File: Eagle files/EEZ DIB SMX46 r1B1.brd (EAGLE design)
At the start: 146 x 95 mm, 157 parts, among them IC1 STM32F030C6T6, IC2 74HC1G126DBVT, IC3 M24C32-WMN6P, IC4 LP2985-33DBVR, IC5 74HC2G04GW,125, K1 FTR-C1GA012G-B05, K10 FTR-C1GA012G-B05, K11 FTR-C1GA012G-B05, K12 FTR-C1GA012G-B05, K13 FTR-C1GA012G-B05, K14 FTR-C1GA012G-B05, K15 FTR-C1GA012G-B05, K16 FTR-C1GA012G-B05, K17 FTR-C1GA012G-B05, K18 FTR-C1GA012G-B05, K19 FTR-C1GA012G-B05, K2 FTR-C1GA012G-B05, K20 FTR-C1GA012G-B05, K21 FTR-C1GA012G-B05, K22 FTR-C1GA012G-B05, K23 FTR-C1GA012G-B05, K24 FTR-C1GA012G-B05, K3 FTR-C1GA012G-B05, K4 FTR-C1GA012G-B05, K5 FTR-C1GA012G-B05, K6 FTR-C1GA012G-B05, K7 FTR-C1GA012G-B05, K8 FTR-C1GA012G-B05, K9 FTR-C1GA012G-B05, Q1 2N7002, Q10 2N7002, Q11 2N7002, Q12 2N7002, Q13 2N7002, Q14 2N7002, Q15 2N7002, Q16 2N7002, Q17 2N7002, Q18 2N7002, Q19 2N7002, Q2 2N7002, Q20 2N7002, Q21 2N7002, Q22 2N7002, Q23 2N7002, Q24 2N7002, Q25 2N7002, Q3 2N7002, Q4 2N7002, Q5 2N7002, Q6 2N7002, Q7 2N7002, Q8 2N7002, Q9 2N7002, X1 N.C., X2 77317-104-28LF, X3 691327310016, X4 691327310016

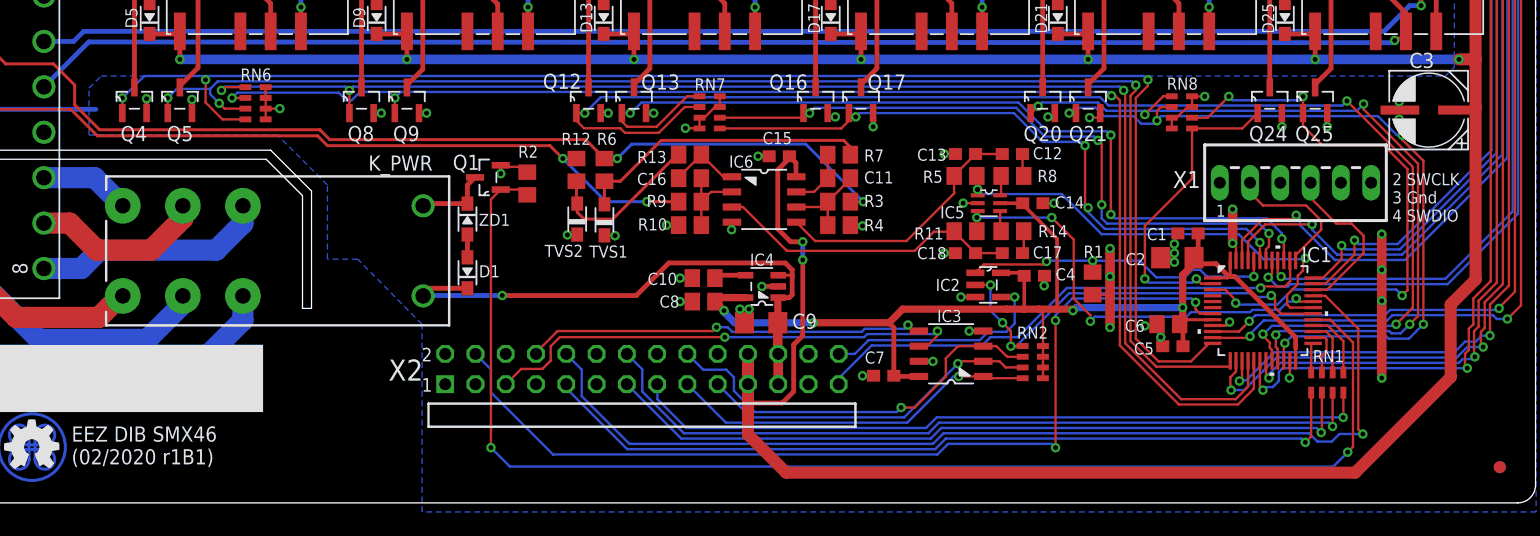
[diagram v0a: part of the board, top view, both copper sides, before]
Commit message: UART relocated
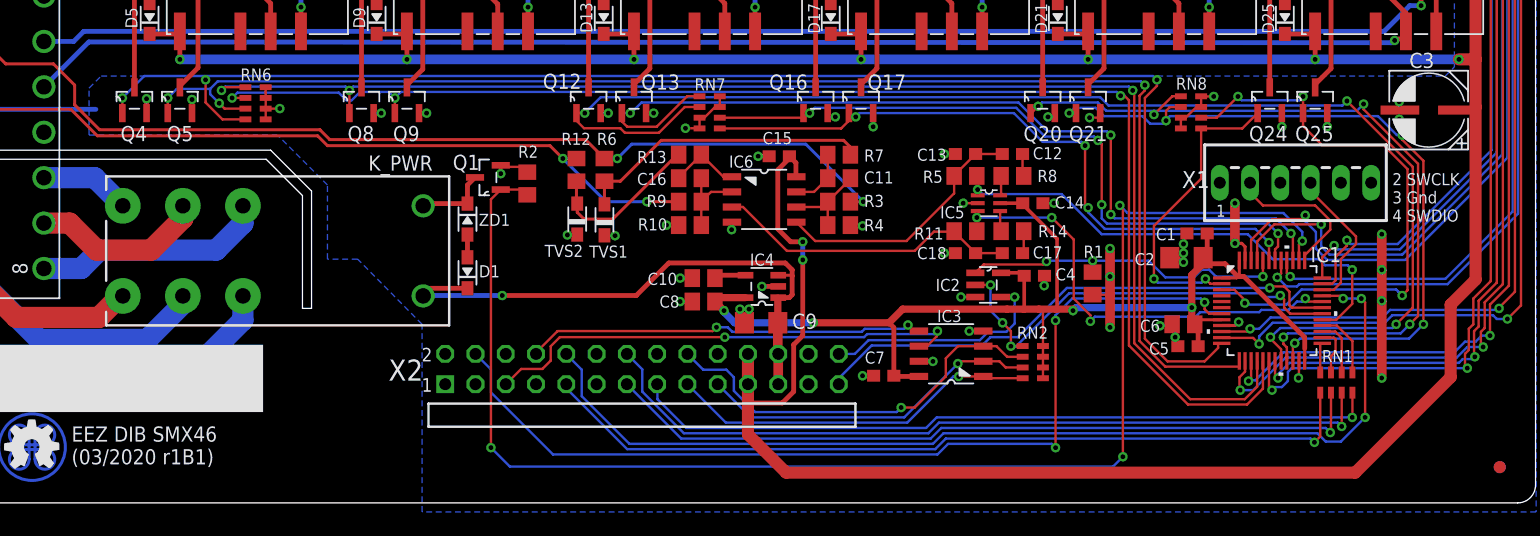
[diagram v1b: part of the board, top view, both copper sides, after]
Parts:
- IC6: value (none) -> OPA2170
- moved C5 1.27 mm to (116.8, 13.1)
- moved C6 1.27 mm to (116.5, 15.0)
- moved C1 0.76 mm to (117.6, 22.6)
- moved C2 0.76 mm to (116.7, 20.6)
- moved IC1 0.76 mm to (123.9, 16.1)
- moved RN1 0.76 mm to (129.3, 10.1)
- moved RN8 0.76 mm to (117.1, 32.8)
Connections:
- net K_PWR: now also IC1.38; no longer IC1.29
- net PWM#1: now also IC1.29; no longer IC1.31
- net UART_RX: now also IC1.31; no longer IC1.38
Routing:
- net K_PWR: track 111.0 -> 118.3 mm, vias 2 -> 4
- net PWM#1: track 38.4 -> 41.8 mm, vias 3 -> 2
- net UART_RX: track 43.5 -> 45.7 mm
- net SWDIO: track 14.0 -> 12.3 mm
- net OUT23: track 51.9 -> 50.3 mm
- net OUT18: track 67.1 -> 65.9 mm
- net +3V3: track 103.0 -> 104.2 mm
- net GND: track 127.1 -> 128.2 mm
- net OUT19: track 63.0 -> 62.0 mm
- net OUT2: track 124.4 -> 125.4 mm
- net SWCLK: track 12.0 -> 12.8 mm
- net OUT9: track 204.0 -> 203.3 mm
- net OUT8: track 187.2 -> 186.5 mm
- net OUT7: track 115.1 -> 115.8 mm
- net OUT6: track 116.4 -> 117.1 mm
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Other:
- board text added: "EEZ DIB SMX46 (03/2020 r1B1)"
- board text added: "EEZ DIB SMX46 (03/2020 r1B1) Project source code: github.com/eez-open"
- board text removed: "EEZ DIB SMX46 (02/2020 r1B1)"
- board text removed: "EEZ DIB SMX46 (02/2020 r1B1) Project source code: github.com/eez-open"

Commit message: debug connector update
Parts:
- X1: value N.C. -> SSW-106-02-S-S; device EEZ_connectors:22-23-2061 -> con-samtec:SSW-106-02-S-S
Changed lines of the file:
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@@
 <attribute name="VALUE" x="94.9071" y="17.907" size="0.6096" layer="27" ratio="10" rot="SR0"/>
 </element>
-<element name="X1" library="EEZ_connectors" package="22-23-2061" value="N.C." x="125.857" y="26.8605" smashed="yes">
-<attribute name="OC_NEWARK" value="27C1933" x="125.857" y="26.8605" size="1.016" layer="27" ratio="10" display="off"/>
-<attribute name="MPN" value="22-23-2061" x="125.857" y="26.8605" size="1.016" layer="27" ratio="10" display="off"/>
-<attribute name="MF" value="MOLEX" x="125.857" y="26.8605" size="1.016" layer="27" ratio="10" display="off"/>
-<attribute name="OC_FARNELL" value="1462922" x="125.857" y="26.8605" size="1.016" layer="27" ratio="10" display="off"/>
-<attribute name="NAME" x="116.332" y="26.416" size="1.4224" layer="25" ratio="10"/>
-<attribute name="VALUE" x="122.9995" y="24.003" size="1.016" layer="27" ratio="10"/>
-</element>
 <element name="RN3" library="EEZ_Lib1" package="CAY16" value="DR1206-47K-4/8" x="57.658" y="89.408" smashed="yes" rot="R90">
 <attribute name="NAME" x="56.4515" y="91.186" size="1.016" layer="25" ratio="10"/>
@@
 <element name="FM2" library="EEZ_Lib1" package="FIDUCIAL_DUAL" value="FIDUCIAL_2" x="143" y="3"/>
 <element name="FM1" library="EEZ_Lib1" package="FIDUCIAL_DUAL" value="FIDUCIAL_2" x="16" y="92"/>
+<element name="X1" library="con-samtec" package="SSW-106-02-S-S" value="SSW-106-02-S-S" x="125.857" y="26.8605" smashed="yes">
+<attribute name="OC_NEWARK" value="11P9416" x="125.857" y="26.8605" size="1.016" layer="27" ratio="10" display="off"/>
+<attribute name="MPN" value="SSW-106-02-S-S" x="125.857" y="26.8605" size="1.016" layer="27" ratio="10" display="off"/>
+<attribute name="MF" value="" x="125.857" y="26.8605" size="1.016" layer="27" ratio="10" display="off"/>
+<attribute name="OC_FARNELL" value="unknown" x="125.857" y="26.8605" size="1.016" layer="27" ratio="10" display="off"/>
+<attribute name="NAME" x="118.11" y="27.4955" size="1.27" layer="25" ratio="10" rot="R180"/>
+<attribute name="VALUE" x="135.382" y="25.5905" size="1.27" layer="27" rot="R90"/>
+</element>
 </elements>
 <signals>
@@
 <contactref element="X4" pad="10"/>
 <contactref element="X4" pad="12"/>
-<contactref element="X1" pad="3"/>
 <contactref element="RN5" pad="4"/>
 <contactref element="RN3" pad="2"/>
@@
 <wire x1="121.6279" y1="21.5011" x2="121.3485" y2="21.7805" width="0.254" layer="1"/>
 <wire x1="121.3485" y1="21.7805" x2="120.777" y2="21.7805" width="0.254" layer="1"/>
+<contactref element="X1" pad="3"/>
 </signal>
 <signal name="N$13">
@@
 <signal name="SWDIO">
 <contactref element="IC1" pad="34"/>
-<contactref element="X1" pad="4"/>
 <wire x1="128.1049" y1="17.8816" x2="129.0701" y2="17.8816" width="0.2032" layer="1"/>
 <wire x1="129.0701" y1="17.8816" x2="129.667" y2="18.4785" width="0.2032" layer="1"/>
@@
 <wire x1="127.127" y1="26.8605" x2="127.127" y2="26.162" width="0.2032" layer="1"/>
 <wire x1="127.127" y1="26.162" x2="130.937" y2="22.352" width="0.2032" layer="1"/>
+<contactref element="X1" pad="4"/>
 </signal>
 <signal name="UART_RX">
@@
 <signal name="SWCLK">
 <contactref element="IC1" pad="37"/>
-<contactref element="X1" pad="2"/>
 <wire x1="126.6317" y1="20.3454" x2="126.6317" y2="20.7772" width="0.2032" layer="1"/>
 <wire x1="126.6317" y1="20.7772" x2="128.778" y2="22.9235" width="0.2032" layer="1"/>
@@
 <wire x1="122.047" y1="26.035" x2="122.047" y2="26.8605" width="0.2032" layer="1"/>
 <wire x1="127.508" y1="24.9555" x2="128.778" y2="23.6855" width="0.2032" layer="1"/>
+<contactref element="X1" pad="2"/>
 </signal>
 <signal name="DIB_NRESET">

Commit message: PCB terminals position adjusted
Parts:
- moved X3 2.20 mm to (12.3, 65.0)
- moved X4 2.20 mm to (12.3, 33.0)
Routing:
- net GND: track 128.2 -> 132.8 mm
- net N$7: track 148.9 -> 151.1 mm
- net N$34: track 117.7 -> 119.9 mm
- net N$16: track 139.4 -> 141.6 mm
- net N$14: track 83.1 -> 85.3 mm
- net N$12: track 139.4 -> 141.6 mm
- net N$11: track 153.7 -> 155.9 mm
- net N$10: track 153.7 -> 155.9 mm
- net N$1: track 63.2 -> 65.4 mm
- net N$95: track 30.3 -> 32.5 mm
- net N$94: track 7.60 -> 9.80 mm
- net N$84: track 19.7 -> 21.9 mm
- net N$82: track 14.8 -> 17.0 mm
- net N$25: track 101.4 -> 103.6 mm
- net N$24: track 101.6 -> 103.8 mm
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
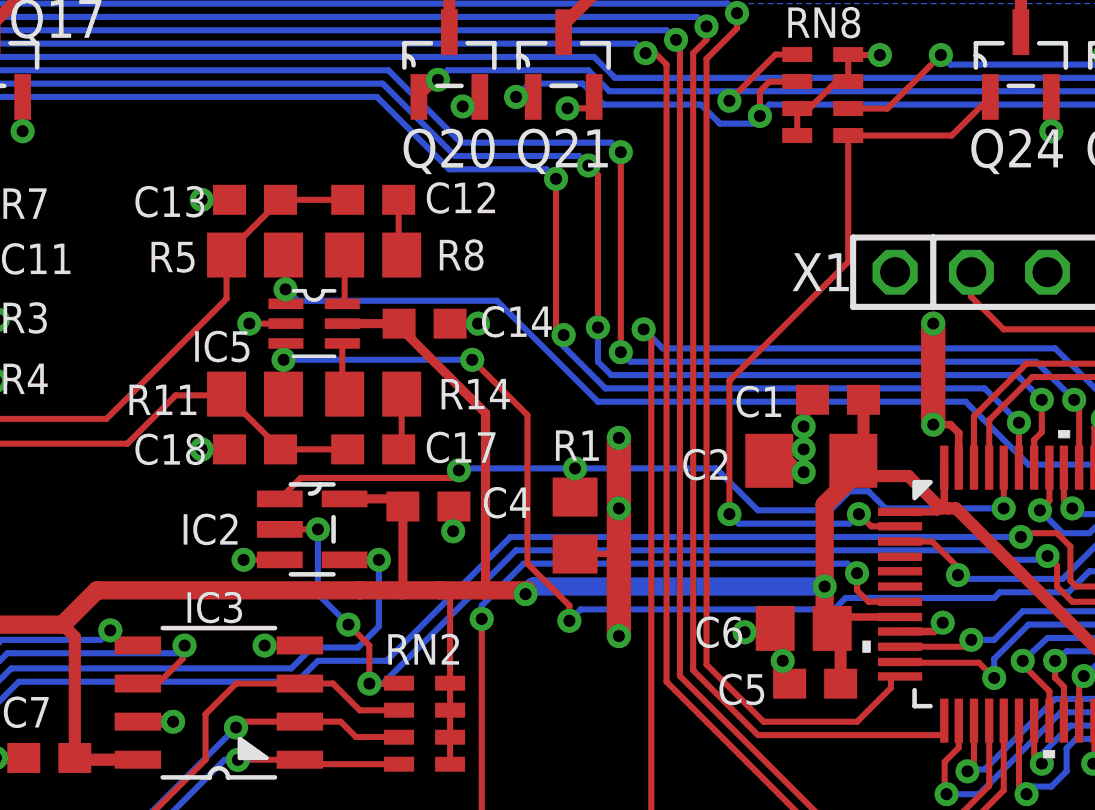
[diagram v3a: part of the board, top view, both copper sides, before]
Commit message: IC2 package update
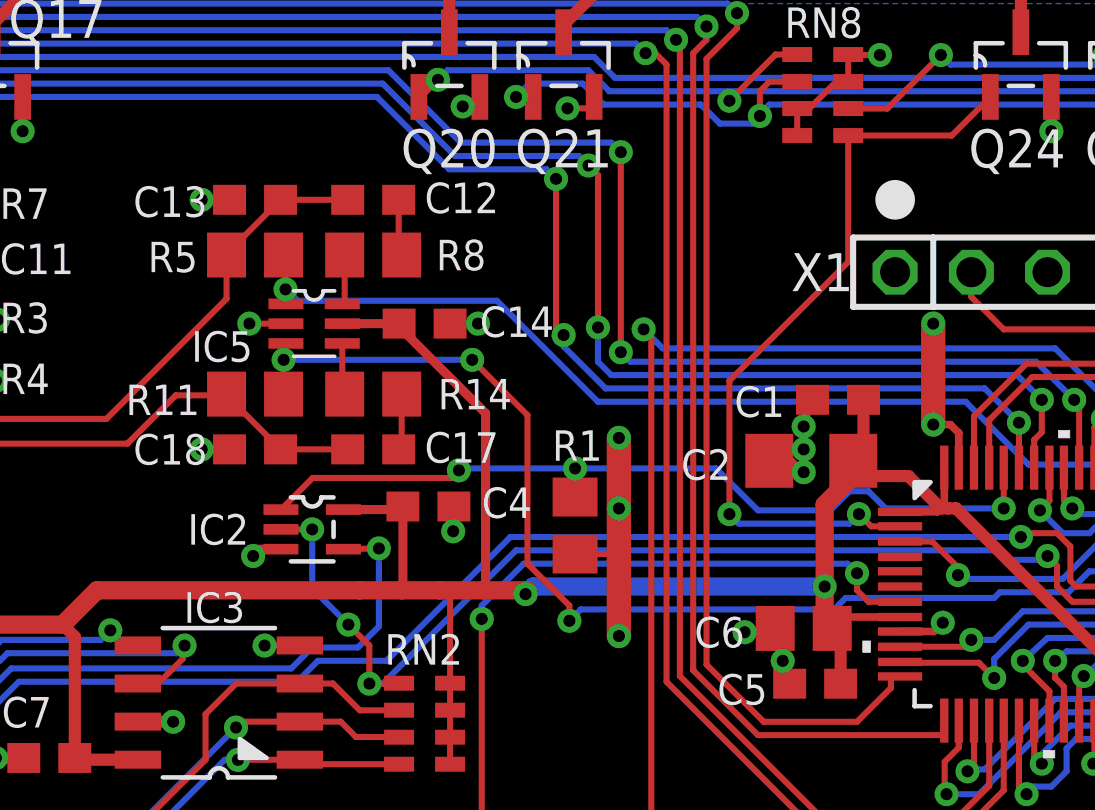
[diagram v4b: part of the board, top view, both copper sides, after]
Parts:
- IC2: value 74HC1G126DBVT -> 74HC1G126GW,125; device EEZ_TI:SOT23-5 -> EEZ_Lib1:SOT65P210X110-5N
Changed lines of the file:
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@@
 <layer number="20" name="Dimension" color="12" fill="1" visible="yes" active="yes"/>
 <layer number="21" name="tPlace" color="7" fill="1" visible="yes" active="yes"/>
-<layer number="22" name="bPlace" color="6" fill="1" visible="yes" active="yes"/>
+<layer number="22" name="bPlace" color="6" fill="1" visible="no" active="yes"/>
 <layer number="23" name="tOrigins" color="15" fill="1" visible="yes" active="yes"/>
 <layer number="24" name="bOrigins" color="15" fill="1" visible="no" active="yes"/>
@@
 4 SWDIO
 </text>
+<circle x="119.507" y="29.2735" radius="0.3302" width="0.6604" layer="21"/>
 </plain>
 <attributes>
@@
 <attribute name="VALUE" x="102.489" y="18.542" size="1.016" layer="27" ratio="10"/>
 </element>
-<element name="IC2" library="EEZ_TI" package="SOT23-5" value="74HC1G126DBVT" x="100.076" y="18.288" smashed="yes">
-<attribute name="NAME" x="95.6691" y="17.78" size="1.016" layer="25" ratio="10" rot="SR0"/>
-<attribute name="VALUE" x="94.9071" y="17.907" size="0.6096" layer="27" ratio="10" rot="SR0"/>
+<element name="IC2" library="EEZ_Lib1" package="SOT65P210X110-5N" value="74HC1G126GW,125" x="100.076" y="18.288" smashed="yes">
+<attribute name="NAME" x="95.9231" y="17.78" size="1.016" layer="25" ratio="10" rot="SR0"/>
+<attribute name="VALUE" x="94.0816" y="18.034" size="0.6096" layer="27" ratio="10" rot="SR0"/>
 </element>
 <element name="RN3" library="EEZ_Lib1" package="CAY16" value="DR1206-47K-4/8" x="57.658" y="89.408" smashed="yes" rot="R90">
@@
 <via x="96.393" y="29.2735" extent="1-16" drill="0.4" shape="square"/>
 <wire x1="97.321" y1="29.2735" x2="96.393" y2="29.2735" width="0.2032" layer="1"/>
-<via x="97.79" y="17.272" extent="1-16" drill="0.4" shape="square"/>
+<via x="98.1075" y="17.399" extent="1-16" drill="0.4" shape="square"/>
 <via x="96.393" y="20.955" extent="1-16" drill="0.4" shape="square"/>
 <wire x1="97.321" y1="20.955" x2="96.393" y2="20.955" width="0.2032" layer="1"/>
-<wire x1="98.9965" y1="17.272" x2="97.79" y2="17.272" width="0.2032" layer="1"/>
 <wire x1="90.463" y1="10.668" x2="89.535" y2="10.668" width="0.4064" layer="1"/>
 <via x="95.4405" y="11.8745" extent="1-16" drill="0.4" shape="square"/>
@@
 <wire x1="8.8265" y1="41.5925" x2="8.8265" y2="33.0835" width="0.4064" layer="16"/>
 <wire x1="8.8265" y1="33.0835" x2="8.89" y2="33.02" width="0.4064" layer="16"/>
+<wire x1="99.0346" y1="17.6276" x2="98.1075" y2="17.6276" width="0.3048" layer="1"/>
+<wire x1="98.1075" y1="17.6276" x2="98.1075" y2="17.399" width="0.3048" layer="1"/>
 </signal>
 <signal name="N$13">
@@
 <wire x1="78.8035" y1="15.113" x2="77.9145" y2="16.002" width="0.6096" layer="16"/>
 <wire x1="77.9145" y1="16.002" x2="77.9145" y2="16.129" width="0.6096" layer="16"/>
-<wire x1="101.1555" y1="19.304" x2="102.8455" y2="19.304" width="0.3048" layer="1"/>
-<wire x1="102.8455" y1="19.304" x2="103.0995" y2="19.05" width="0.3048" layer="1"/>
 <wire x1="102.9725" y1="25.146" x2="102.997" y2="25.146" width="0.3048" layer="1"/>
 <wire x1="102.9725" y1="25.146" x2="101.0793" y2="25.146" width="0.3048" layer="1"/>
@@
 <wire x1="117.69" y1="13.1445" x2="117.69" y2="14.705" width="0.4064" layer="1"/>
 <wire x1="117.69" y1="14.705" x2="117.409" y2="14.986" width="0.4064" layer="1"/>
+<wire x1="101.1174" y1="18.9484" x2="103.0995" y2="18.9484" width="0.3048" layer="1"/>
+<wire x1="103.0995" y1="18.9484" x2="103.0995" y2="19.05" width="0.3048" layer="1"/>
 </signal>
 <signal name="N$70">
@@
 <wire x1="117.983" y1="19.558" x2="118.618" y2="19.558" width="0.2032" layer="16"/>
 <wire x1="119.1895" y1="18.9865" x2="118.618" y2="19.558" width="0.2032" layer="16"/>
-<wire x1="104.7115" y1="20.0025" x2="99.695" y2="20.0025" width="0.2032" layer="1"/>
-<wire x1="99.695" y1="20.0025" x2="98.9965" y2="19.304" width="0.2032" layer="1"/>
 <wire x1="104.7115" y1="20.0025" x2="104.9655" y2="20.2565" width="0.2032" layer="1"/>
 <wire x1="123.1265" y1="18.9865" x2="119.1895" y2="18.9865" width="0.2032" layer="16"/>
@@
 <wire x1="108.839" y1="20.32" x2="105.029" y2="20.32" width="0.2032" layer="16"/>
 <wire x1="105.029" y1="20.32" x2="104.9655" y2="20.2565" width="0.2032" layer="16"/>
+<wire x1="104.7115" y1="20.0025" x2="100.0887" y2="20.0025" width="0.2032" layer="1"/>
+<wire x1="100.0887" y1="20.0025" x2="99.0346" y2="18.9484" width="0.2032" layer="1"/>
 </signal>
 <signal name="DIB_CSA">
@@
 <wire x1="102.9725" y1="13.161" x2="102.7595" y2="13.161" width="0.2032" layer="1"/>
 <via x="101.2825" y="15.113" extent="1-16" drill="0.4" shape="octagon"/>
-<via x="100.2665" y="18.288" extent="1-16" drill="0.4" shape="octagon"/>
-<wire x1="100.2665" y1="18.288" x2="98.9965" y2="18.288" width="0.2032" layer="1"/>
+<via x="100.076" y="18.288" extent="1-16" drill="0.4" shape="octagon"/>
+<wire x1="100.076" y1="18.288" x2="99.0346" y2="18.288" width="0.2032" layer="1"/>
 <via x="101.981" y="13.1445" extent="1-16" drill="0.4" shape="octagon"/>
 <wire x1="102.7595" y1="13.161" x2="102.743" y2="13.1445" width="0.2032" layer="1"/>
@@
 <wire x1="123.3805" y1="17.272" x2="124.46" y2="17.272" width="0.2032" layer="16"/>
 <wire x1="124.46" y1="17.272" x2="124.587" y2="17.399" width="0.2032" layer="16"/>
-<wire x1="100.2665" y1="18.288" x2="100.2665" y2="16.129" width="0.2032" layer="16"/>
-<wire x1="100.2665" y1="16.129" x2="101.2825" y2="15.113" width="0.2032" layer="16"/>
+<wire x1="100.2665" y1="16.129" x2="100.5205" y2="15.875" width="0.2032" layer="16"/>
+<wire x1="100.5205" y1="15.875" x2="101.2825" y2="15.113" width="0.2032" layer="16"/>
 <wire x1="101.981" y1="13.1445" x2="101.981" y2="14.4145" width="0.2032" layer="1"/>
 <wire x1="101.981" y1="14.4145" x2="101.2825" y2="15.113" width="0.2032" layer="1"/>
@@
 <wire x1="106.8705" y1="17.5895" x2="102.4255" y2="13.1445" width="0.2032" layer="16"/>
 <wire x1="102.4255" y1="13.1445" x2="101.981" y2="13.1445" width="0.2032" layer="16"/>
+<wire x1="100.076" y1="18.288" x2="100.076" y2="16.3195" width="0.2032" layer="16"/>
+<wire x1="100.076" y1="16.3195" x2="100.2665" y2="16.129" width="0.2032" layer="16"/>
 </signal>
 <signal name="SWDIO">
@@
 <wire x1="87.54" y1="12.5" x2="88.8905" y2="12.5" width="0.2032" layer="16"/>
 <wire x1="88.8905" y1="12.5" x2="90.043" y2="13.6525" width="0.2032" layer="16"/>
-<via x="102.2985" y="17.272" extent="1-16" drill="0.4" shape="octagon"/>
-<wire x1="102.2985" y1="17.272" x2="101.1555" y2="17.272" width="0.2032" layer="1"/>
+<via x="102.2985" y="17.653" extent="1-16" drill="0.4" shape="octagon"/>
+<wire x1="102.2985" y1="17.653" x2="101.1174" y2="17.6276" width="0.2032" layer="1"/>
 <wire x1="99.3775" y1="13.6525" x2="90.043" y2="13.6525" width="0.2032" layer="16"/>
 <wire x1="102.2985" y1="15.0495" x2="101.6" y2="14.351" width="0.2032" layer="16"/>
 <wire x1="101.6" y1="14.351" x2="100.076" y2="14.351" width="0.2032" layer="16"/>
 <wire x1="100.076" y1="14.351" x2="99.3775" y2="13.6525" width="0.2032" layer="16"/>
-<wire x1="102.2985" y1="17.272" x2="102.2985" y2="15.0495" width="0.2032" layer="16"/>
+<wire x1="102.2985" y1="17.653" x2="102.2985" y2="15.0495" width="0.2032" layer="16"/>
 </signal>
 <signal name="N$86">
